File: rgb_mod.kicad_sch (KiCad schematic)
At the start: 29 parts, among them IC1 Micom, IC2 Jungle AN5693K, J2 Jumper_2_Bridged, J3 Jumper_2_Bridged, J4 Jumper_2_Bridged, J5 Jumper_2_Bridged, J6 Term, J7 Jumper_2_Bridged

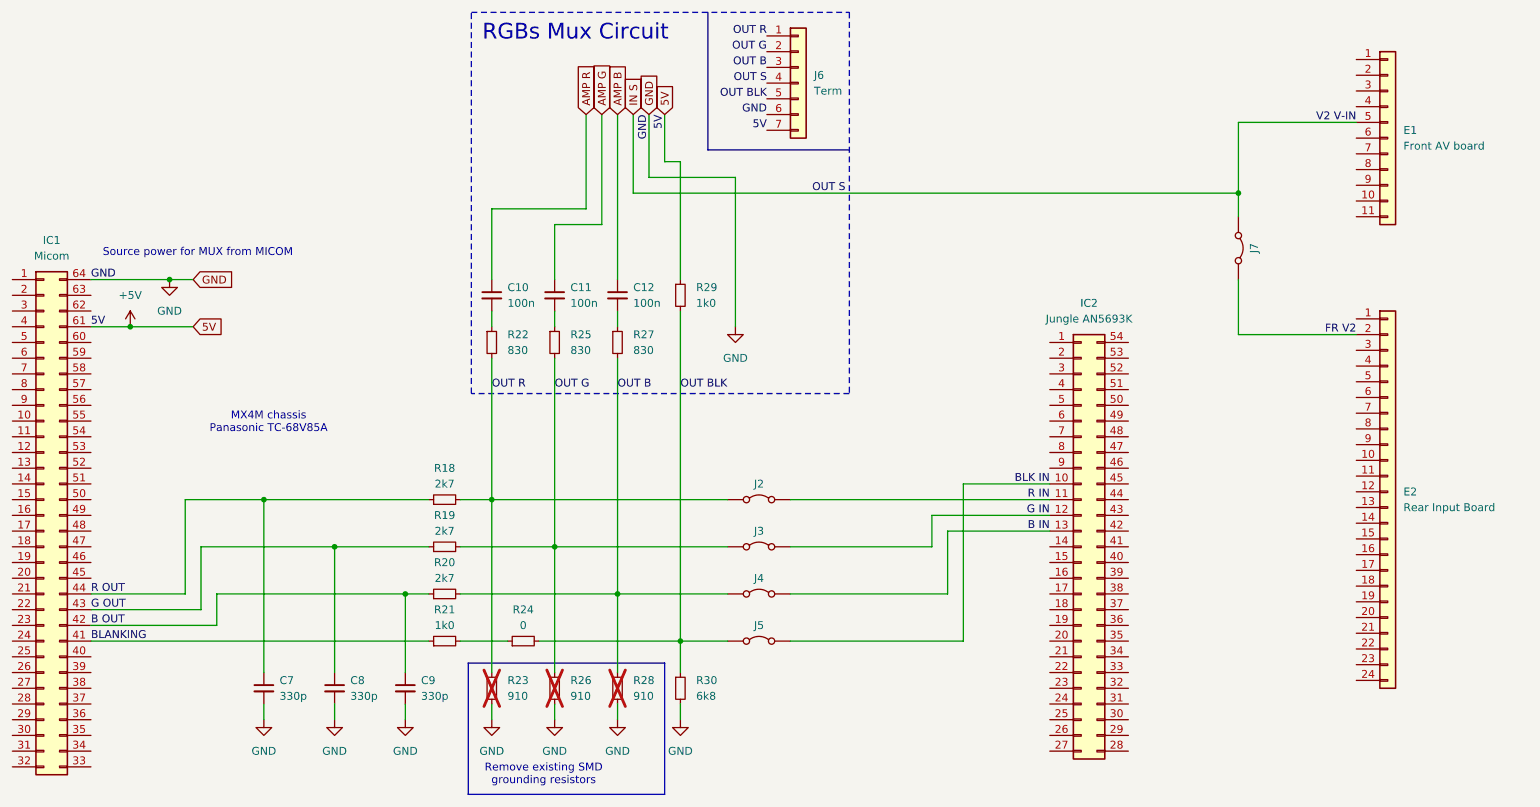
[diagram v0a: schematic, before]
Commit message: second design for nec tv and with inputs integrated
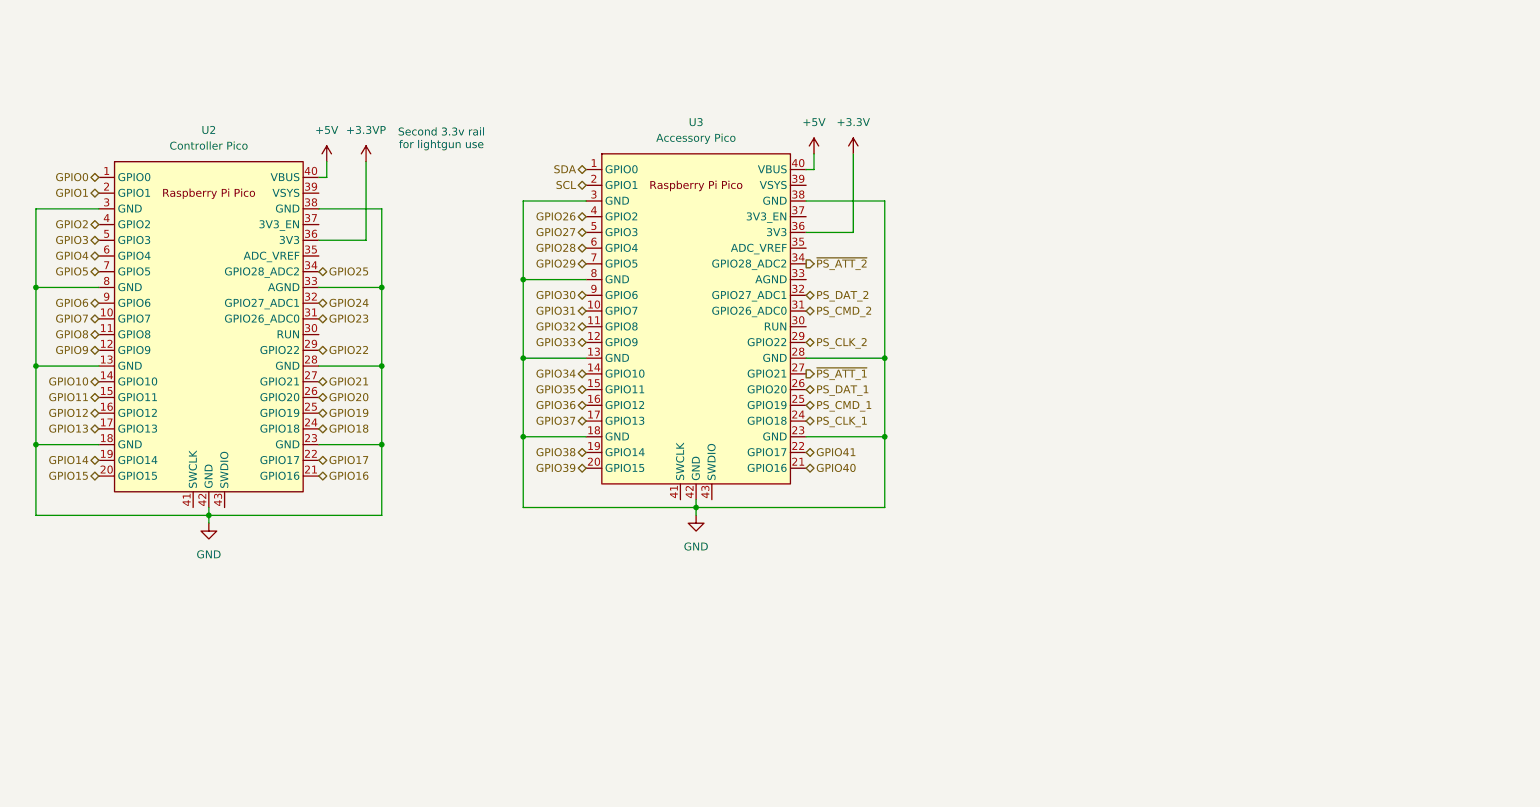
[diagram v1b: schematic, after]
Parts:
- removed C10, C11, C12: 100n, Capacitor_THT:C_Disc_D6.0mm_W2.5mm_P5.00mm, symbol Device:C_Small
- removed C7, C8, C9: 330p, symbol Device:C_Small
- removed E1: Front AV board, symbol Connector_Generic:Conn_01x11
- removed E2: Rear Input Board, symbol Connector_Generic:Conn_01x24
- removed IC1: Micom, symbol Connector_Generic:Conn_02x32_Counter_Clockwise
- removed IC2: Jungle AN5693K, symbol Connector_Generic:Conn_02x27_Counter_Clockwise
- removed J2, J3, J4, J5, J7: Jumper_2_Bridged, symbol Jumper:Jumper_2_Bridged
- removed J6: Term, TerminalBlock_Altech:Altech_AK100_1x07_P5.00mm, symbol Connector_Generic:Conn_01x07
- removed R18, R19, R20: 2k7, symbol Device:R_Small
- removed R21: 1k0, symbol Device:R_Small
- removed R22, R25, R27: 830, Resistor_THT:R_Axial_DIN0204_L3.6mm_D1.6mm_P7.62mm_Horizontal, symbol Device:R_Small
- removed R23, R26, R28: 910, symbol Device:R_Small
- removed R24: 0, symbol Device:R_Small
- removed R29: 1k0, Resistor_THT:R_Axial_DIN0204_L3.6mm_D1.6mm_P7.62mm_Horizontal, symbol Device:R_Small
- removed R30: 6k8, symbol Device:R_Small
- added U2: Controller Pico, KiCad Components:RPi_Pico_SMD_TH, symbol MCU_RaspberryPi_and_Boards:Pico
- added U3: Accessory Pico, KiCad Components:RPi_Pico_SMD_TH, symbol MCU_RaspberryPi_and_Boards:Pico
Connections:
- net +5V: now also U2.40 (VBUS), U3.40 (VBUS)
- net GND: now also U2.13 (GND), U2.18 (GND), U2.23 (GND), U2.28 (GND), U2.3 (GND), U2.33 (AGND), U2.38 (GND), U2.42 (GND), U2.8 (GND), U3.13 (GND), U3.18 (GND), U3.23 (GND), U3.28 (GND), U3.3 (GND), U3.38 (GND), U3.42 (GND), U3.8 (GND)
- new net +3.3V: U3.36 (3V3)
- new net +3.3VP: U2.36 (3V3)
- new net GPIO0: U2.1 (GPIO0)
- new net GPIO1: U2.2 (GPIO1)
- new net GPIO10: U2.14 (GPIO10)
- new net GPIO11: U2.15 (GPIO11)
- new net GPIO12: U2.16 (GPIO12)
- new net GPIO13: U2.17 (GPIO13)
- new net GPIO14: U2.19 (GPIO14)
- new net GPIO15: U2.20 (GPIO15)
- new net GPIO16: U2.21 (GPIO16)
- new net GPIO17: U2.22 (GPIO17)
- new net GPIO18: U2.24 (GPIO18)
- new net GPIO19: U2.25 (GPIO19)
- new net GPIO2: U2.4 (GPIO2)
- new net GPIO20: U2.26 (GPIO20)
- new net GPIO21: U2.27 (GPIO21)
- new net GPIO22: U2.29 (GPIO22)
- new net GPIO23: U2.31 (GPIO26_ADC0)
- new net GPIO24: U2.32 (GPIO27_ADC1)
- new net GPIO25: U2.34 (GPIO28_ADC2)
- new net GPIO26: U3.4 (GPIO2)
- new net GPIO27: U3.5 (GPIO3)
- new net GPIO28: U3.6 (GPIO4)
- new net GPIO29: U3.7 (GPIO5)
- new net GPIO3: U2.5 (GPIO3)
- new net GPIO30: U3.9 (GPIO6)
- new net GPIO31: U3.10 (GPIO7)
- new net GPIO32: U3.11 (GPIO8)
- new net GPIO33: U3.12 (GPIO9)
- new net GPIO34: U3.14 (GPIO10)
- new net GPIO35: U3.15 (GPIO11)
- new net GPIO36: U3.16 (GPIO12)
- new net GPIO37: U3.17 (GPIO13)
- new net GPIO38: U3.19 (GPIO14)
- new net GPIO39: U3.20 (GPIO15)
- new net GPIO4: U2.6 (GPIO4)
- new net GPIO40: U3.21 (GPIO16)
- new net GPIO41: U3.22 (GPIO17)
- new net GPIO5: U2.7 (GPIO5)
- new net GPIO6: U2.9 (GPIO6)
- new net GPIO7: U2.10 (GPIO7)
- new net GPIO8: U2.11 (GPIO8)
- new net GPIO9: U2.12 (GPIO9)
- new net PS_CLK_1: U3.24 (GPIO18)
- new net PS_CLK_2: U3.29 (GPIO22)
- new net PS_CMD_1: U3.25 (GPIO19)
- new net PS_CMD_2: U3.31 (GPIO26_ADC0)
- new net PS_DAT_1: U3.26 (GPIO20)
- new net PS_DAT_2: U3.32 (GPIO27_ADC1)
- new net SCL: U3.2 (GPIO1)
- new net SDA: U3.1 (GPIO0)
- new net ~{PS_ATT_1}: U3.27 (GPIO21)
- new net ~{PS_ATT_2}: U3.34 (GPIO28_ADC2)
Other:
- note added: "Second 3.3v rail for lightgun use"
- note removed: "MX4M chassis Panasonic TC-68V85A"
- note removed: "RGBs Mux Circuit"
- note removed: "Remove existing SMD grounding resistors"
- note removed: "Source power for MUX from MICOM"
